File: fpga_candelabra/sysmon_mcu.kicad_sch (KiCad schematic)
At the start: 43 parts, among them J1 TYPE-C-31-M-12, J2 DNP/MCU_DEBUG, U17 GD25Q80EEIG, U35 SN74LVC1T45DCK, U38 SN74LVC1T45DCK, U39 SN74LVC1T45DCK, U8 RP2040, Y1 12MHz 10pF

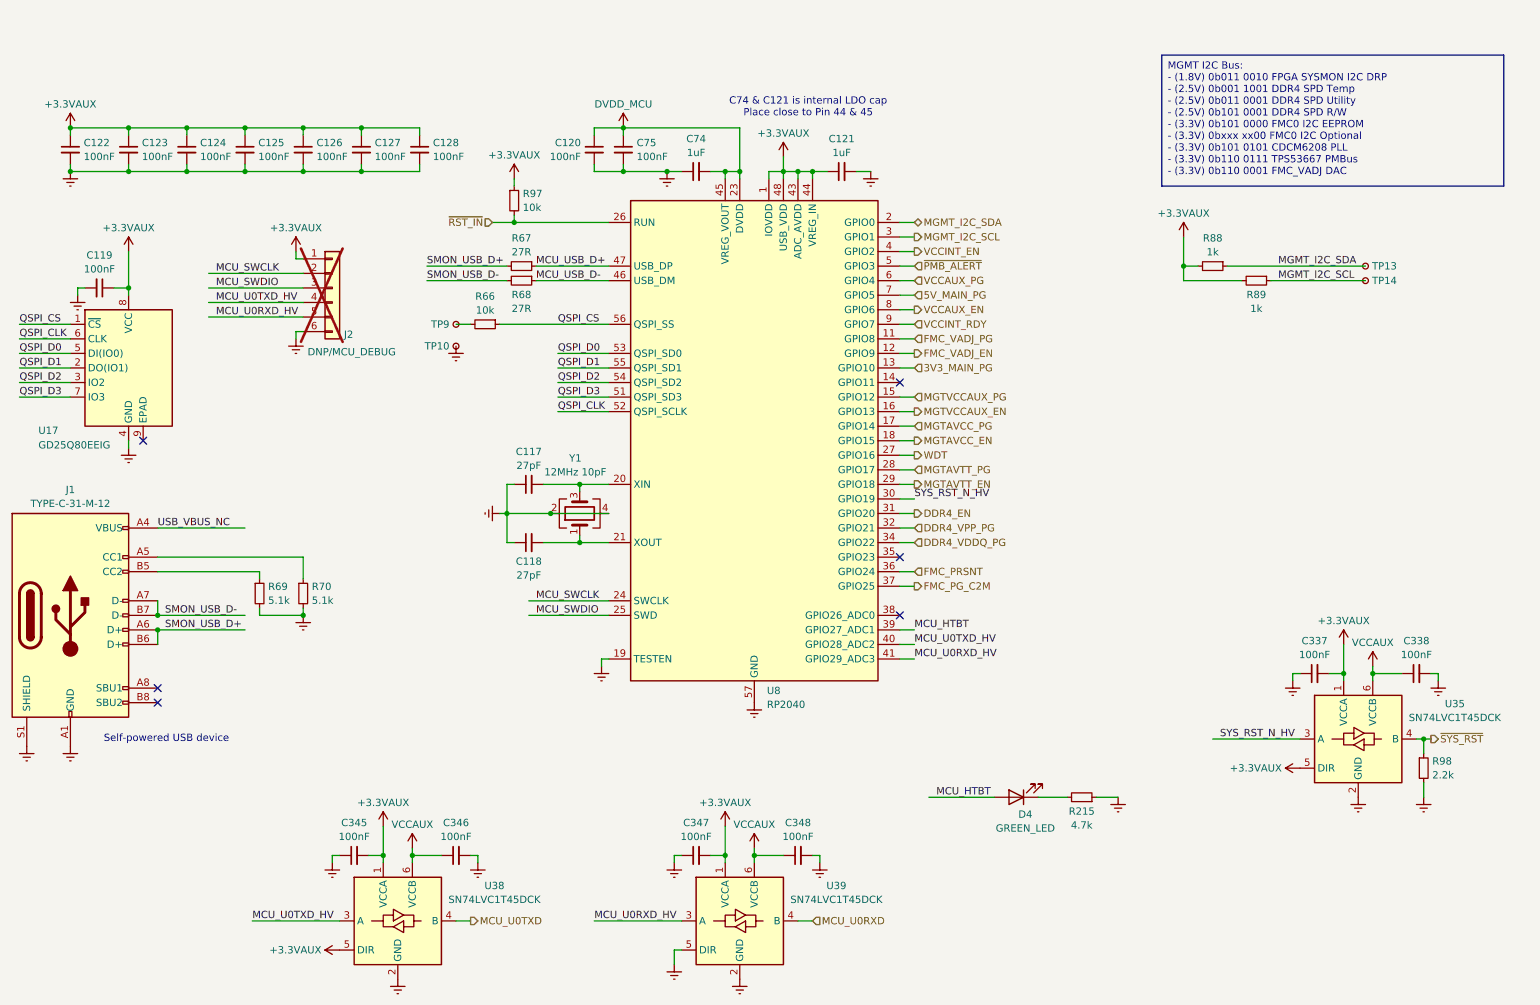
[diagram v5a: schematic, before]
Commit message: fpga_candelabra: more bugfixes & improvements for rev 0.2.0
- Add Digilent JTAG-SMT2-NC onboard
- Add fan controller & 4pin fan header
- Use 9pin header for USB2.0
- Misc fixes for structure

Signed-off-by: Yichuan Gao <gaoyichuan000@gmail.com>
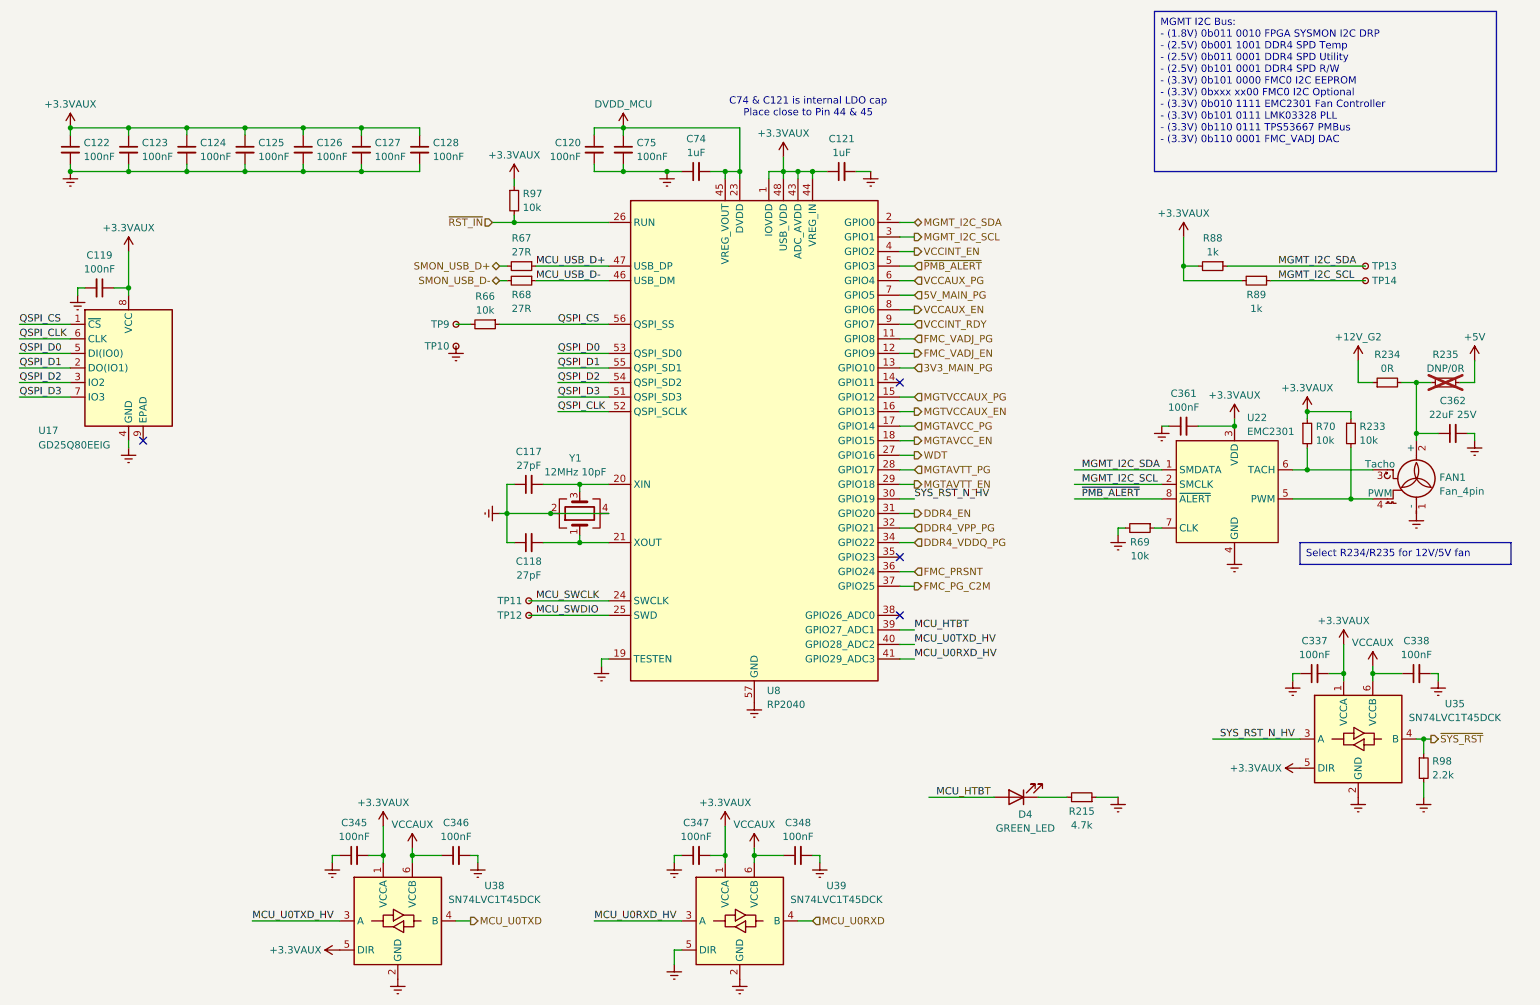
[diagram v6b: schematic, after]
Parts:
- removed J1: TYPE-C-31-M-12, Connector_USB:USB_C_Receptacle_HRO_TYPE-C-31-M-12, symbol Connector:USB_C_Receptacle_USB2.0_16P
- removed J2: DNP/MCU_DEBUG, Connector_PinHeader_2.00mm:PinHeader_1x06_P2.00mm_Vertical, symbol Connector_Generic:Conn_01x06
- added C361: 100nF, Capacitor_SMD:C_0402_1005Metric, symbol Device:C_Small
- added C362: 22uF 25V, Capacitor_SMD:C_1206_3216Metric, symbol Device:C_Small
- added FAN1: Fan_4pin, Connector:FanPinHeader_1x04_P2.54mm_Vertical, symbol Motor:Fan_4pin
- added R233: 10k, Resistor_SMD:R_0402_1005Metric, symbol Device:R_Small
- added R234: 0R, Resistor_SMD:R_0402_1005Metric, symbol Device:R_Small
- added R235: DNP/0R, Resistor_SMD:R_0402_1005Metric, symbol Device:R_Small
- added TP11, TP12: TestPoint_Small, TestPoint:TestPoint_Pad_D1.0mm, symbol Connector:TestPoint_Small
- added U22: EMC2301, Package_SO:MSOP-8_3x3mm_P0.65mm, symbol CHIPSAlliance_Interface:EMC2301
- R69, R70: value 5.1k -> 10k
- TP13, TP14: footprint TestPoint:TestPoint_Pad_D1.0mm -> TestPoint:TestPoint_THTPad_D1.0mm_Drill0.5mm
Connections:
- net +3.3VAUX: now also R70.1, C361.2, R233.1, U22.3 (VDD)
- net Earth: now also C361.1, C362.2, FAN1.1 (-), U22.4 (GND); no longer R70.2
- net MCU_SWCLK: now also TP11.1
- net MCU_SWDIO: now also TP12.1
- net MGMT_I2C_SCL: now also U22.2 (SMCLK)
- net MGMT_I2C_SDA: now also U22.1 (SMDATA)
- net ~{PMB_ALERT}: now also U22.8 (~{ALERT})
- net at R69.1: now also U22.7 (CLK)
- new net: C362.1, FAN1.2 (+), R234.2, R235.1
- new net: FAN1.4 (PWM), R233.2, U22.5 (PWM)
- new net: FAN1.3 (Tacho), R70.2, U22.6 (TACH)
- new net +12V_G2: R234.1
- new net +5V: R235.2
- no-connect marks 6 -> 4
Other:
- note removed: "Self-powered USB device"

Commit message: fpga_candelabra: add author & rev to schematics
Signed-off-by: Yichuan Gao <gaoyichuan000@gmail.com>
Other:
- company: (none) -> CHIPS Alliance
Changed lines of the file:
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@@
 	(title_block
 		(title "System Monitor RP2040 MCU")
+		(date "2025-02-05")
+		(rev "0.2.0")
+		(company "CHIPS Alliance")
+		(comment 1 "Yichuan Gao")
+		(comment 2 "Yichuan Gao")
 	)
 	(junction

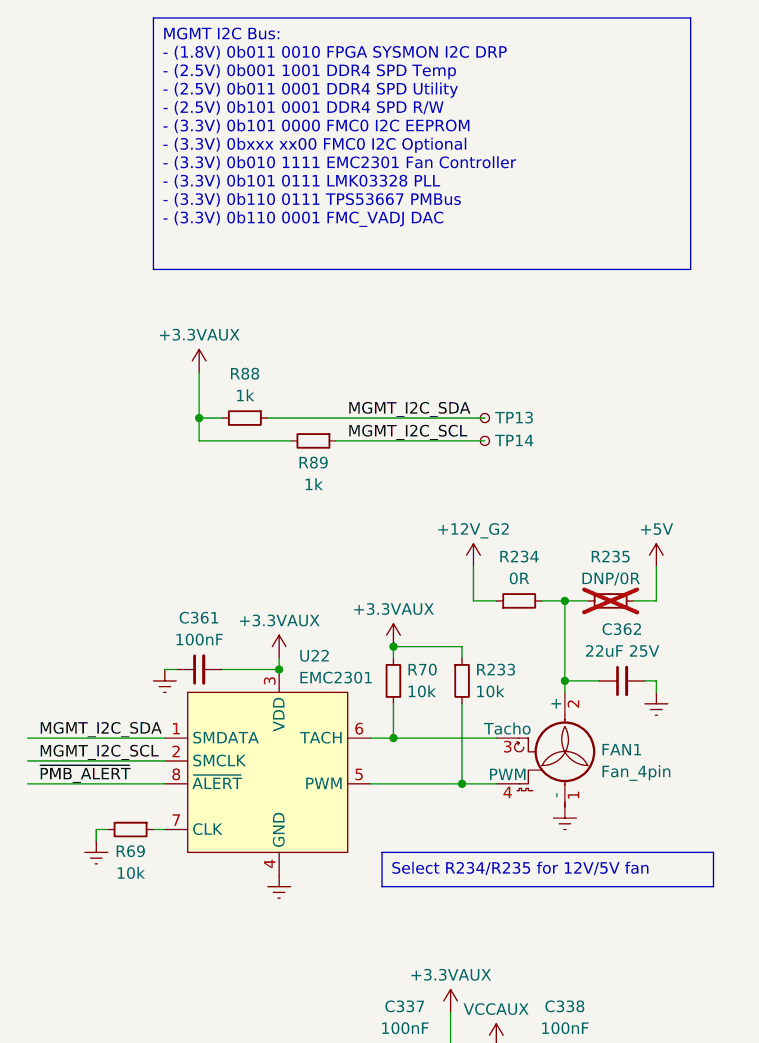
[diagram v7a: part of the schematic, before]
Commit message: fpga_candelabra: update to kicad 9.0
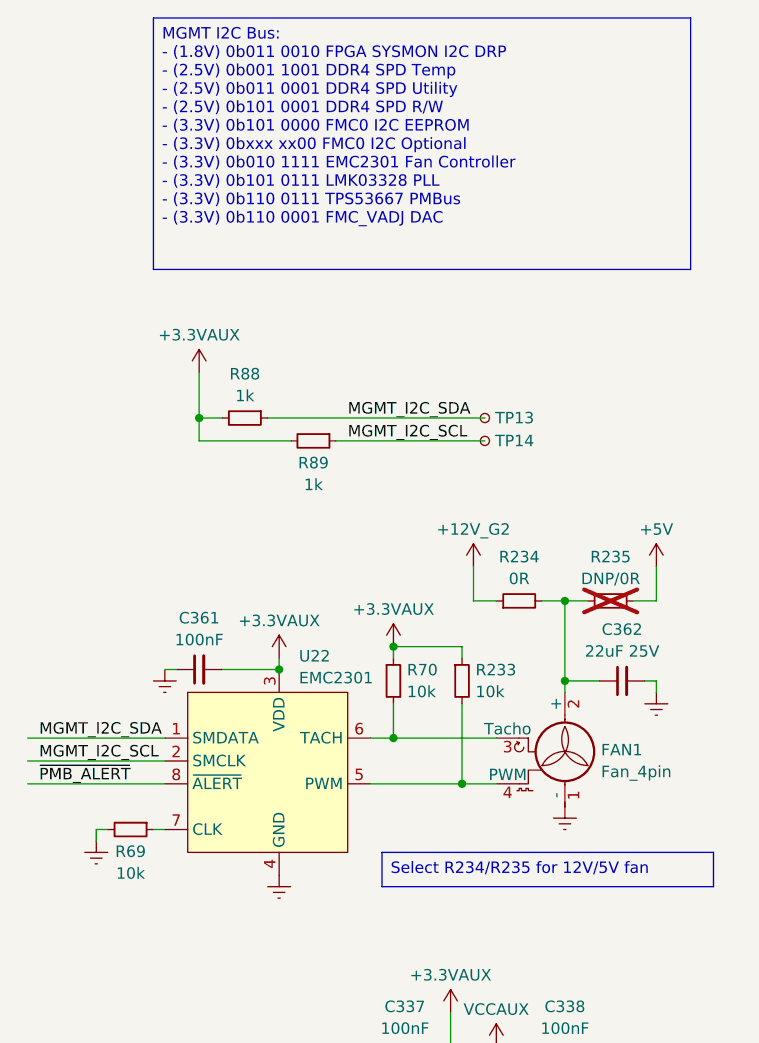
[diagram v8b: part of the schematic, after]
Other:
- company: CHIPS Alliance -> Sipeed
